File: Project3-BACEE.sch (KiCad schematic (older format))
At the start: 0 parts

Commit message: added symbol footprints
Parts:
- added BT?: Battery, symbol Device:Battery
- added C? (x2): C, symbol Device:C
- added C?: CP, symbol Device:CP
- added D?: LED, symbol Device:LED
- added R? (x2): R, symbol Device:R
- added U?: 24LC1025, symbol Memory_EEPROM:24LC1025
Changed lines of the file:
@@
 $Descr A4 11693 8268
 encoding utf-8
-Sheet 1 1
+Sheet 1 2
 Title "BACEE"
 Date "2021-11-26"
@@
 Comment4 ""
 $EndDescr
+$Comp
+L Device:Battery BT?
+U 1 1 61A18C0A
+P 2275 2500
+F 0 "BT?" H 2383 2546 50  0000 L CNN
+F 1 "Battery" H 2383 2455 50  0000 L CNN
+F 2 "" V 2275 2560 50  0001 C CNN
+F 3 "~" V 2275 2560 50  0001 C CNN
+	1    2275 2500
+	1    0    0    -1
+$EndComp
+$Comp
+L Device:C C?
+U 1 1 61A19A4D
+P 3675 2350
+F 0 "C?" H 3790 2396 50  0000 L CNN
+F 1 "C" H 3790 2305 50  0000 L CNN
+F 2 "" H 3713 2200 50  0001 C CNN
+F 3 "~" H 3675 2350 50  0001 C CNN
+	1    3675 2350
+	1    0    0    -1
+$EndComp
+$Comp
+L Device:C C?
+U 1 1 61A1A1BD
+P 3675 2900
+F 0 "C?" H 3790 2946 50  0000 L CNN
+F 1 "C" H 3790 2855 50  0000 L CNN
+F 2 "" H 3713 2750 50  0001 C CNN
+F 3 "~" H 3675 2900 50  0001 C CNN
+	1    3675 2900
+	1    0    0    -1
+$EndComp
+$Comp
+L Device:CP C?
+U 1 1 61A1ACBD
+P 3675 3625
+F 0 "C?" H 3793 3671 50  0000 L CNN
+F 1 "CP" H 3793 3580 50  0000 L CNN
+F 2 "" H 3713 3475 50  0001 C CNN
+F 3 "~" H 3675 3625 50  0001 C CNN
+	1    3675 3625
+	1    0    0    -1
+$EndComp
+$Comp
+L Device:LED D?
+U 1 1 61A1B764
+P 5125 2500
+F 0 "D?" H 5118 2717 50  0000 C CNN
+F 1 "LED" H 5118 2626 50  0000 C CNN
+F 2 "" H 5125 2500 50  0001 C CNN
+F 3 "~" H 5125 2500 50  0001 C CNN
+	1    5125 2500
+	1    0    0    -1
+$EndComp
+$Comp
+L Device:R R?
+U 1 1 61A1BA7E
+P 5625 3325
+F 0 "R?" H 5695 3371 50  0000 L CNN
+F 1 "R" H 5695 3280 50  0000 L CNN
+F 2 "" V 5555 3325 50  0001 C CNN
+F 3 "~" H 5625 3325 50  0001 C CNN
+	1    5625 3325
+	1    0    0    -1
+$EndComp
+$Comp
+L Device:R R?
+U 1 1 61A1C043
+P 5625 3875
+F 0 "R?" H 5695 3921 50  0000 L CNN
+F 1 "R" H 5695 3830 50  0000 L CNN
+F 2 "" V 5555 3875 50  0001 C CNN
+F 3 "~" H 5625 3875 50  0001 C CNN
+	1    5625 3875
+	1    0    0    -1
+$EndComp
+$Comp
+L Memory_EEPROM:24LC1025 U?
+U 1 1 61A1CEED
+P 7550 2525
+F 0 "U?" H 7550 3006 50  0000 C CNN
+F 1 "24LC1025" H 7550 2915 50  0000 C CNN
+F 2 "" H 7550 2525 50  0001 C CNN
+F 3 "http://ww1.microchip.com/downloads/en/DeviceDoc/21941B.pdf" H 7550 2525 50  0001 C CNN
+	1    7550 2525
+	1    0    0    -1
+$EndComp
+$Sheet
+S 7175 3925 2375 1525
+U 61A1FED7
+F0 "Connectors" 50
+F1 "Connectors.sch" 50
+$EndSheet
 $EndSCHEMATC

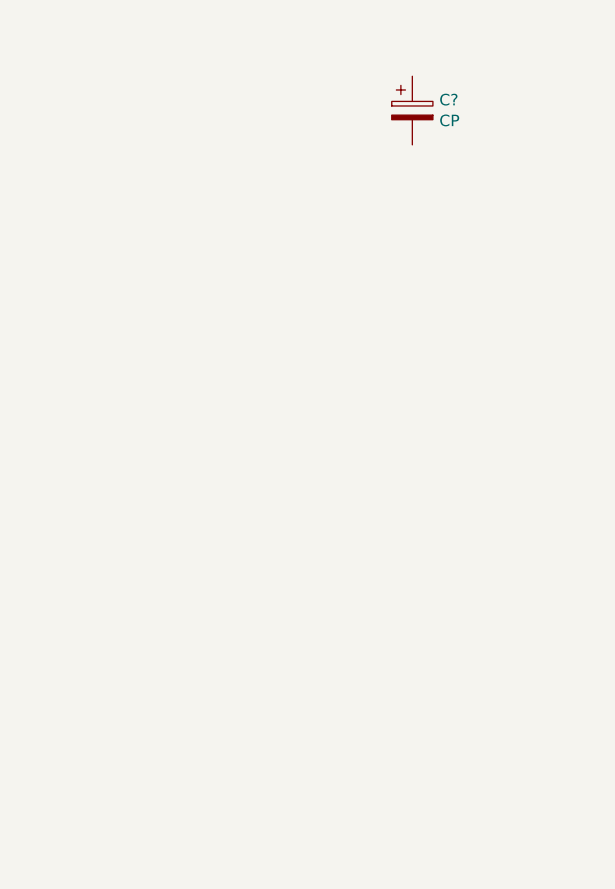
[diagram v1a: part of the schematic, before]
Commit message: added atMega3228P
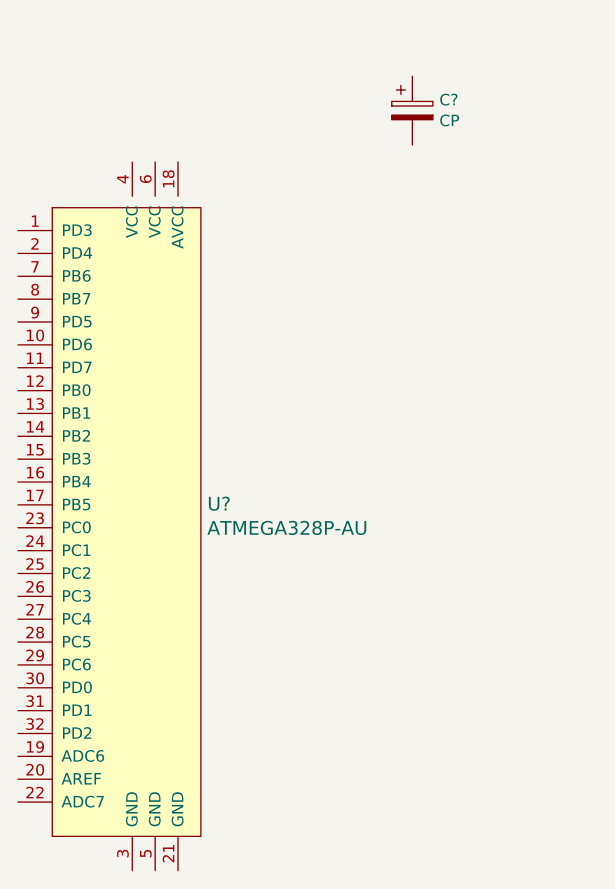
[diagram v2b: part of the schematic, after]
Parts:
- added U?: ATMEGA328P-AU, digikey-footprints:TQFP-32_7x7mm, symbol dk_Embedded-Microcontrollers:ATMEGA328P-AU
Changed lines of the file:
@@
 F1 "Connectors.sch" 50
 $EndSheet
+$Comp
+L dk_Embedded-Microcontrollers:ATMEGA328P-AU U?
+U 1 1 61A26237
+P 2450 5450
+F 0 "U?" H 2778 5553 60  0000 L CNN
+F 1 "ATMEGA328P-AU" H 2778 5447 60  0000 L CNN
+F 2 "digikey-footprints:TQFP-32_7x7mm" H 2650 5650 60  0001 L CNN
+F 3 "http://www.microchip.com/mymicrochip/filehandler.aspx?ddocname=en608326" H 2650 5750 60  0001 L CNN
+F 4 "ATMEGA328P-AU-ND" H 2650 5850 60  0001 L CNN "Digi-Key_PN"
+F 5 "ATMEGA328P-AU" H 2650 5950 60  0001 L CNN "MPN"
+F 6 "Integrated Circuits (ICs)" H 2650 6050 60  0001 L CNN "Category"
+F 7 "Embedded - Microcontrollers" H 2650 6150 60  0001 L CNN "Family"
+F 8 "http://www.microchip.com/mymicrochip/filehandler.aspx?ddocname=en608326" H 2650 6250 60  0001 L CNN "DK_Datasheet_Link"
+F 9 "/product-detail/en/microchip-technology/ATMEGA328P-AU/ATMEGA328P-AU-ND/1832260" H 2650 6350 60  0001 L CNN "DK_Detail_Page"
+F 10 "IC MCU 8BIT 32KB FLASH 32TQFP" H 2650 6450 60  0001 L CNN "Description"
+F 11 "Microchip Technology" H 2650 6550 60  0001 L CNN "Manufacturer"
+F 12 "Active" H 2650 6650 60  0001 L CNN "Status"
+	1    2450 5450
+	1    0    0    -1
+$EndComp
 $EndSCHEMATC

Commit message: added custom symbol
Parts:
- added U?: DS1337_CSP, symbol project3:DS1337_CSP
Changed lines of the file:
@@
+	1    0    0    -1
+$EndComp
+$Comp
+L project3:DS1337_CSP U?
+U 1 1 61A2C2A1
+P 4975 5175
+F 0 "U?" H 5000 5706 50  0000 C CNN
+F 1 "DS1337_CSP" H 5000 5615 50  0000 C CNN
+F 2 "" H 4975 5975 50  0001 C CNN
+F 3 "" H 4975 5975 50  0001 C CNN
+	1    4975 5175
 	1    0    0    -1
 $EndComp

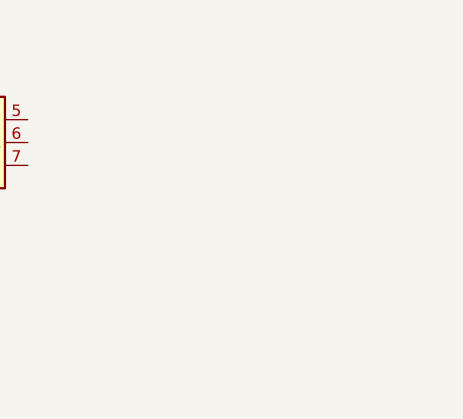
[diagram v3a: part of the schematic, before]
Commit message: added crystals
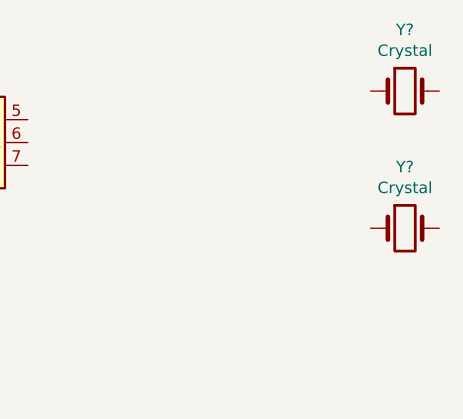
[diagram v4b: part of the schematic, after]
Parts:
- added Y? (x2): Crystal, symbol Device:Crystal
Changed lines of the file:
@@
+	1    0    0    -1
+$EndComp
+$Comp
+L Device:Crystal Y?
+U 1 1 61A2DC0F
+P 9600 2300
+F 0 "Y?" H 9600 2568 50  0000 C CNN
+F 1 "Crystal" H 9600 2477 50  0000 C CNN
+F 2 "" H 9600 2300 50  0001 C CNN
+F 3 "~" H 9600 2300 50  0001 C CNN
+	1    9600 2300
+	1    0    0    -1
+$EndComp
+$Comp
+L Device:Crystal Y?
+U 1 1 61A2E8DA
+P 9600 2900
+F 0 "Y?" H 9600 3168 50  0000 C CNN
+F 1 "Crystal" H 9600 3077 50  0000 C CNN
+F 2 "" H 9600 2900 50  0001 C CNN
+F 3 "~" H 9600 2900 50  0001 C CNN
+	1    9600 2900
 	1    0    0    -1
 $EndComp
